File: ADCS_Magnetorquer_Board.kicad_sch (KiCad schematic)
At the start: 0 parts

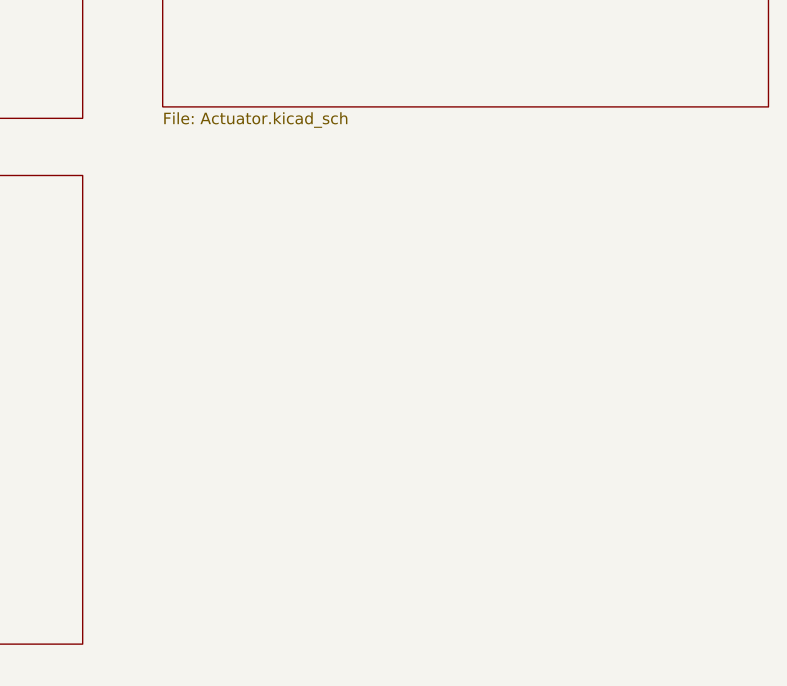
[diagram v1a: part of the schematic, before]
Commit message: Added debug schematic sheet and ST-Link 14 pin header
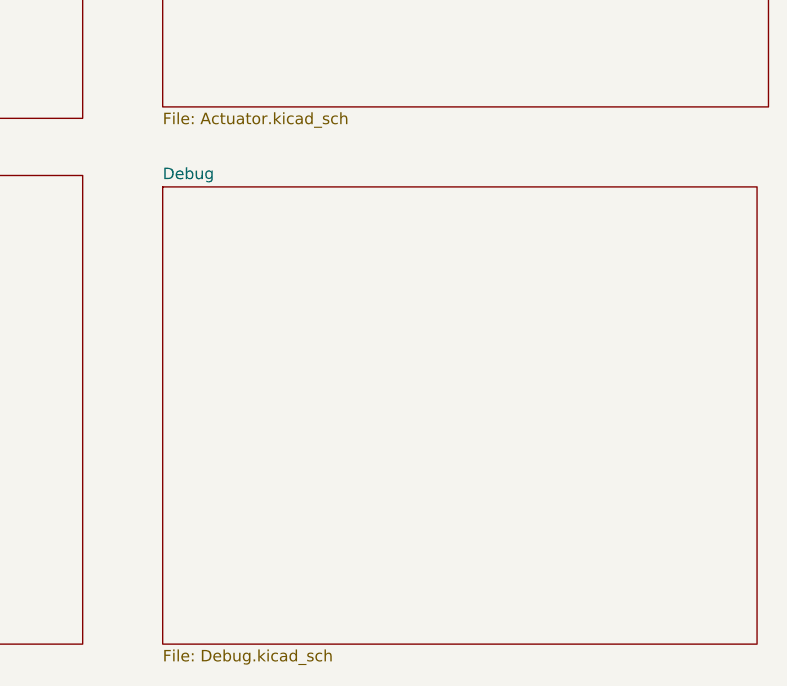
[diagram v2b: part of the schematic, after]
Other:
- added sheet Debug (Debug.kicad_sch)
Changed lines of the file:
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@@
+	)
+	(sheet
+		(at 115.57 69.85)
+		(size 66.04 50.8)
+		(exclude_from_sim no)
+		(in_bom yes)
+		(on_board yes)
+		(dnp no)
+		(fields_autoplaced yes)
+		(stroke
+			(width 0.1524)
+			(type solid)
+		)
+		(fill
+			(color 0 0 0 0)
+		)
+		(property "Sheetname" "Debug"
+			(at 115.57 69.1384 0)
+			(show_name no)
+			(do_not_autoplace no)
+			(effects
+				(font
+					(size 1.27 1.27)
+				)
+				(justify left bottom)
+			)
+		)
+		(property "Sheetfile" "Debug.kicad_sch"
+			(at 115.57 121.2346 0)
+			(show_name no)
+			(do_not_autoplace no)
+			(effects
+				(font
+					(size 1.27 1.27)
+				)
+				(justify left top)
+			)
+		)
+		(instances
+			(project "ADCS_Magnetorquer_Board"
+				(path "/ad8674f1-23de-4bd4-9414-642ec663a6a4"
+					(page "5")
+				)
+			)
+		)
 	)
 	(sheet
